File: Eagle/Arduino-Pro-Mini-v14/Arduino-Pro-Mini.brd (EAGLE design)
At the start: 30 x 31.9 mm, 15 parts, among them Q1 8/16/20MHz, U1 ATMEGA328, U2 MIC5205

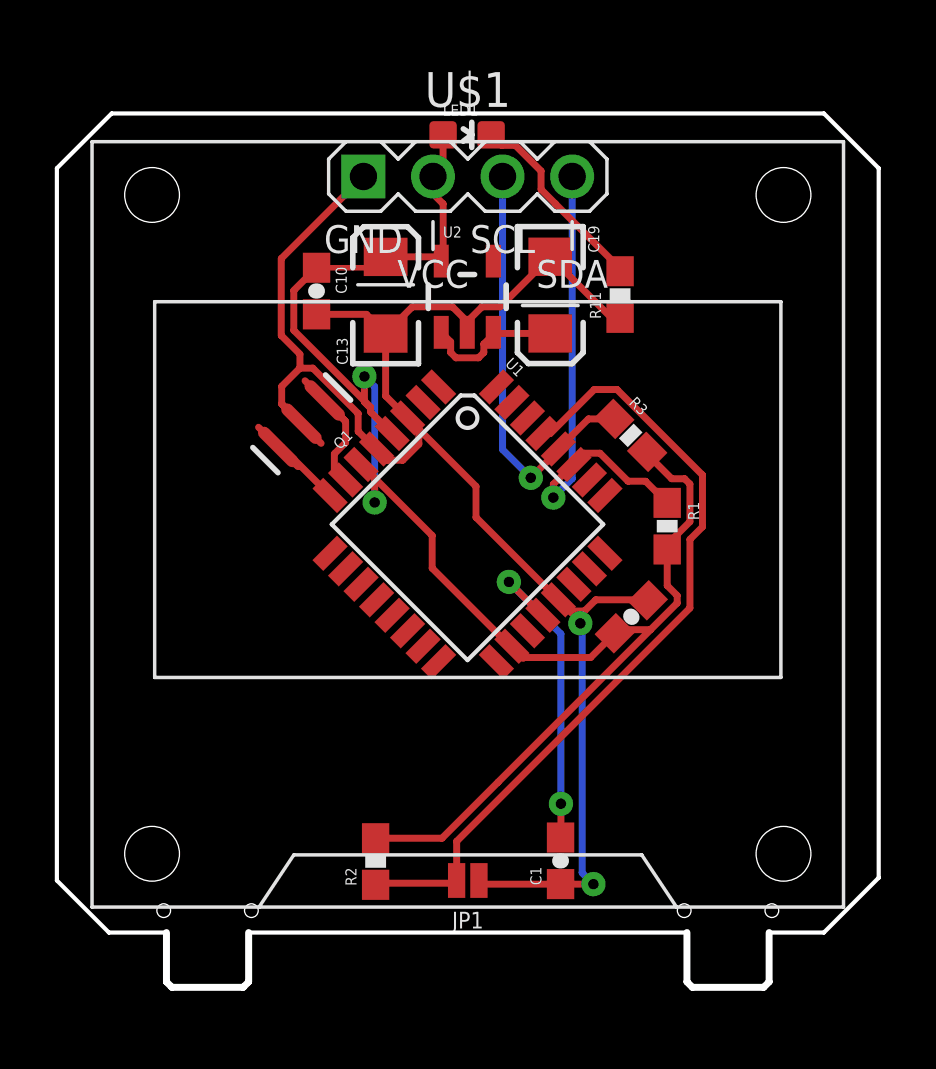
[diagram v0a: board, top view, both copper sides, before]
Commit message: Added LED driers
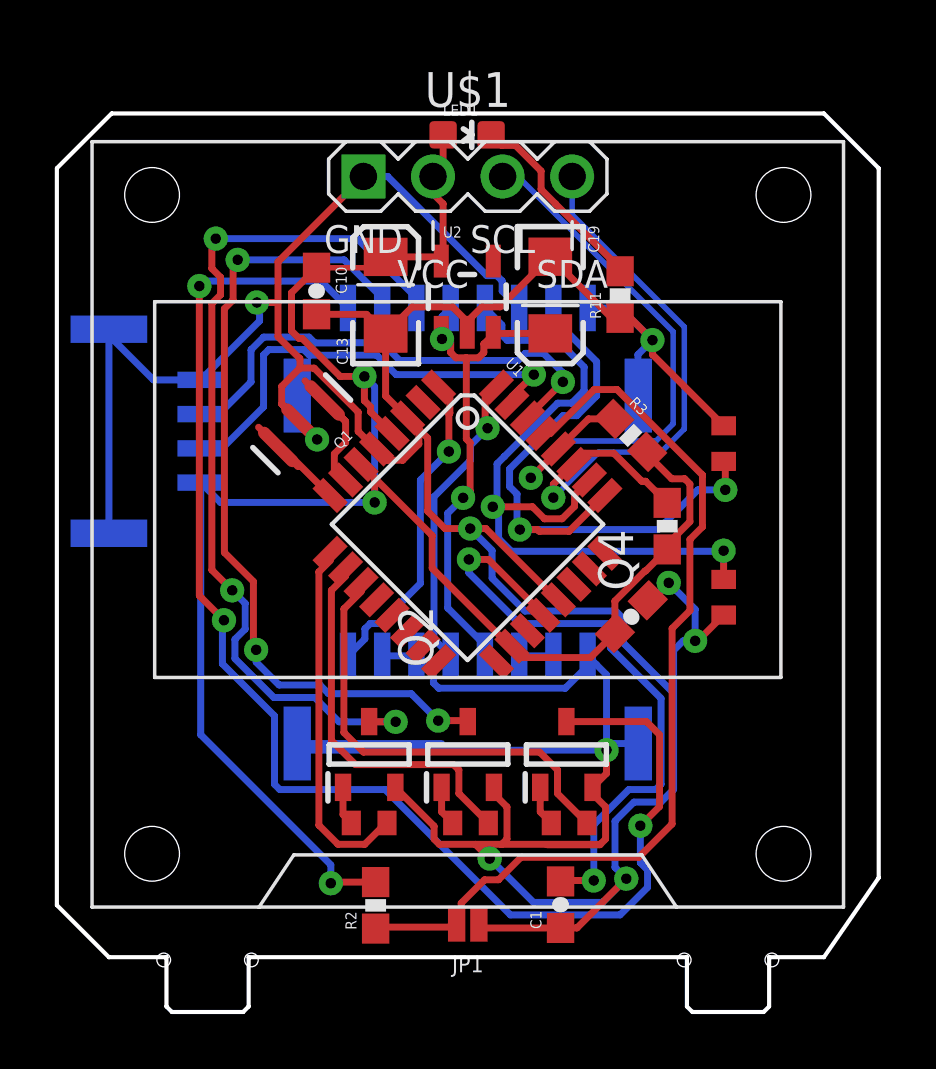
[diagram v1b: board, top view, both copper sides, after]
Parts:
- added J1: BM04B-GHS-TBT(LF)(SN)(N), BM04B-GHS-TBT_LF__SN__N_:JST_BM04B-GHS-TBT(LF)(SN)(N)
- added J2, J3: SM08B-GHS-TB(LF)(SN), SM08B-GHS-TB_LF__SN_:JST_SM08B-GHS-TB(LF)(SN)
- added Q2, Q3, Q4: BCW65CLT1G, BCW65CLT1G:SOT96P237X111-3N
- added R4, R5: 1Mohm, eagle-ltspice:R0402
- added R6, R7, R8: 4.7k, eagle-ltspice:R0402
- R1, R3: value (none) -> 2.2k
- moved C1 1.60 mm to (18.4, 1.12)
- moved JP1 1.60 mm to (15.0, 0.40)
- moved R2 1.60 mm to (11.6, 1.09)
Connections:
- new net B: J3.8, Q4.3
- new net G: J3.7, Q3.3
- new net N$3: Q4.1, R8.1
- new net N$5: Q3.1, R7.1
- new net N$6: Q2.1, R6.1
- new net R: J3.6, Q2.3
- new net RAWIN: C19.A, J2.4, J3.5, U2.1, U2.3
- net A2: now also J3.2, R5.1
- net A3: now also J3.4, R4.1
- net D2: now also J2.5
- net D3: now also J2.8
- net D5: now also R6.2
- net D6: now also R7.2
- net D7: now also R8.2
- net GND: now also J1.1, J1.S1, J1.S2, J2.1, J2.6, J2.7, J2.SH1, J2.SH2, J3.1, J3.3, J3.SH1, J3.SH2, Q2.2, Q3.2, Q4.2, R4.2, R5.2
- net RAW: now also J2.2, J2.3; no longer C19.A, U2.1, U2.3
- net RXI: now also J1.2
- net TXO: now also J1.3
- net VCC: now also J1.4
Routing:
- net GND: track 64.5 -> 171.4 mm, vias 2 -> 9
- net B: track 0.00 -> 50.9 mm, vias 0 -> 3
- net R: track 0.00 -> 32.7 mm, vias 0 -> 3
- net G: track 0.00 -> 30.2 mm, vias 0 -> 3
- net A3: track 0.00 -> 26.8 mm, vias 0 -> 2
- net A2: track 0.00 -> 23.4 mm, vias 0 -> 2
- net RAWIN: track 0.00 -> 18.5 mm, vias 0 -> 2
- net RXI: track 0.00 -> 18.0 mm, vias 0 -> 1
- net TXO: track 0.00 -> 16.5 mm, vias 0 -> 1
- net D7: track 0.00 -> 16.4 mm
- net D6: track 0.00 -> 14.0 mm
- net D5: track 0.00 -> 13.2 mm
- net D3: track 0.00 -> 11.7 mm, vias 0 -> 1
- net D2: track 0.00 -> 11.1 mm, vias 0 -> 1
- net AREF: track 12.0 -> 23.0 mm
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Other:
- board size 30 x 31.9 mm -> 30 x 32.8 mm

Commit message: LED board
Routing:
- net GND: track 171.4 -> 169.5 mm
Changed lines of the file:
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@@
 <drawing>
 <settings>
-<setting alwaysvectorfont="yes"/>
+<setting alwaysvectorfont="no"/>
 <setting keepoldvectorfont="yes"/>
 <setting verticaltext="up"/>
@@
 <wire x1="20.0302" y1="3.513225" x2="19.836775" y2="3.3198" width="0.254" layer="1"/>
 <wire x1="19.836775" y1="3.3198" x2="19.821784375" y2="3.304809375" width="0.254" layer="1"/>
-<wire x1="19.821784375" y1="3.304809375" x2="17.9" y2="3.304809375" width="0.254" layer="1"/>
 <wire x1="19.836775" y1="3.3198" x2="16.236775" y2="3.3198" width="0.254" layer="1"/>
 <wire x1="13.7448" y1="9.213225" x2="13.938225" y2="9.0198" width="0.254" layer="16"/>
@@
 <wire x1="17.411853125" y1="20.467453125" x2="16.6111125" y2="19.6667125" width="0.254" layer="1"/>
 <wire x1="16.6111125" y1="19.6667125" x2="16.6111125" y2="19.4495375" width="0.254" layer="1"/>
-<wire x1="11.67871875" y1="21.1747" x2="9.217275" y2="21.1747" width="0.254" layer="16"/>
+<wire x1="11.67871875" y1="21.1747" x2="9.907275" y2="21.1747" width="0.254" layer="16"/>
 <wire x1="6.033025" y1="17.775" x2="5.25" y2="17.775" width="0.254" layer="16"/>
 <wire x1="12.385965625" y1="20.467453125" x2="11.67871875" y2="21.1747" width="0.254" layer="16"/>
 <wire x1="17.411853125" y1="20.467453125" x2="12.385965625" y2="20.467453125" width="0.254" layer="16"/>
 <wire x1="7.5448" y1="19.286775" x2="6.033025" y2="17.775" width="0.254" layer="16"/>
-<wire x1="9.217275" y1="21.1747" x2="9.011775" y2="21.3802" width="0.254" layer="16"/>
-<wire x1="9.011775" y1="21.3802" x2="7.738225" y2="21.3802" width="0.254" layer="16"/>
+<wire x1="9.907275" y1="21.1747" x2="9.701775" y2="21.3802" width="0.254" layer="16"/>
+<wire x1="9.701775" y1="21.3802" x2="7.738225" y2="21.3802" width="0.254" layer="16"/>
 <wire x1="7.738225" y1="21.3802" x2="7.5448" y2="21.186775" width="0.254" layer="16"/>
 <wire x1="7.5448" y1="21.186775" x2="7.5448" y2="19.286775" width="0.254" layer="16"/>
@@
 <contactref element="U1" pad="30"/>
 <contactref element="J1" pad="2"/>
-<wire x1="7.54884375" y1="21.8374" x2="9.20115625" y2="21.8374" width="0.254" layer="16"/>
-<wire x1="10.70911875" y1="21.625" x2="10.71601875" y2="21.6319" width="0.254" layer="16"/>
-<wire x1="9.41355625" y1="21.625" x2="10.70911875" y2="21.625" width="0.254" layer="16"/>
-<wire x1="9.20115625" y1="21.8374" x2="9.41355625" y2="21.625" width="0.254" layer="16"/>
-<wire x1="10.71601875" y1="21.6319" x2="11.8681" y2="21.6319" width="0.254" layer="16"/>
+<wire x1="7.54884375" y1="21.8374" x2="9.92115625" y2="21.8374" width="0.254" layer="16"/>
+<wire x1="10.12665625" y1="21.6319" x2="11.8681" y2="21.6319" width="0.254" layer="16"/>
+<wire x1="9.92115625" y1="21.8374" x2="10.12665625" y2="21.6319" width="0.254" layer="16"/>
 <wire x1="12.517015625" y1="20.982984375" x2="11.8681" y2="21.6319" width="0.254" layer="16"/>
 <via x="18.4719125" y="20.2" extent="1-16" drill="0.381"/>
@@
 <wire x1="14.569025" y1="21.0797" x2="14.946" y2="21.0797" width="0.254" layer="1"/>
 <wire x1="15.392575" y1="21.0797" x2="15.586" y2="21.273125" width="0.254" layer="1"/>
-<wire x1="14.3756" y1="21.6651" x2="14.3756" y2="21.273125" width="0.254" layer="1"/>
+<wire x1="14.3756" y1="21.273125" x2="14.3756" y2="21.6651" width="0.254" layer="1"/>
 <wire x1="15.586" y1="21.273125" x2="15.586" y2="21.5853" width="0.254" layer="1"/>
 <wire x1="15.586" y1="21.5853" x2="15.9707" y2="21.97" width="0.254" layer="1"/>
-<wire x1="14.0308" y1="22.0099" x2="14.17035" y2="21.87035" width="0.254" layer="1"/>
 <contactref element="J2" pad="4"/>
 <via x="14.83" y="15.97" extent="1-16" drill="0.381"/>
-<wire x1="14.17035" y1="21.87035" x2="14.3756" y2="21.6651" width="0.254" layer="1"/>
 <wire x1="15.625" y1="10.59" x2="15.625" y2="10.2" width="0.254" layer="16"/>
 <wire x1="14.265" y1="11.95" x2="15.625" y2="10.59" width="0.254" layer="16"/>
@@
 <contactref element="J3" pad="5"/>
 <wire x1="14.946" y1="21.0797" x2="15.392575" y2="21.0797" width="0.254" layer="1"/>
-<wire x1="14.375" y1="22.9" x2="14.0581" y2="22.5831" width="0.254" layer="16"/>
-<wire x1="14.0581" y1="22.5831" x2="14.0581" y2="21.7671125" width="0.254" layer="16"/>
+<wire x1="13.9881" y1="22.5131" x2="14.375" y2="22.9" width="0.254" layer="16"/>
+<wire x1="14.3756" y1="21.6651" x2="14.0308" y2="22.0099" width="0.254" layer="1"/>
+<wire x1="14.0308" y1="22.0099" x2="14.0308" y2="21.7944125" width="0.254" layer="1"/>
+<wire x1="14.0308" y1="21.7944125" x2="14.0581" y2="21.7671125" width="0.254" layer="1"/>
 <via x="14.0581" y="21.7671125" extent="1-16" drill="0.381"/>
-<wire x1="14.0581" y1="21.7671125" x2="14.1613375" y2="21.87035" width="0.254" layer="1"/>
-<wire x1="14.1613375" y1="21.87035" x2="14.17035" y2="21.87035" width="0.254" layer="1"/>
+<wire x1="14.0581" y1="21.7671125" x2="13.9881" y2="21.8371125" width="0.254" layer="16"/>
+<wire x1="13.9881" y1="21.8371125" x2="13.9881" y2="22.5131" width="0.254" layer="16"/>
 </signal>
 <signal name="A2">
